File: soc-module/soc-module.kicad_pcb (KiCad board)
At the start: 2 copper layers, 56 x 31 mm, 17 parts, among them J1 Micro_SD_Card_Det_Hirose_DM3AT, J2 Conn_01x13, J3 Conn_01x14, SW1 Prog, SW2 Reset, U1 ATECC608A-SSHDA, U2 ESP32-WROVER-IE-16MB

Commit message: Ongoing
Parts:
- C1: renamed from C1^; value C -> 100nF
- C2, C3, C4: value C -> 100nF
- J1: value Micro_SD_Card_Det_Hirose_DM3AT -> Micro_SD
- J2: value Conn_01x13 -> East; footprint Connector_PinHeader_2.54mm:PinHeader_1x13_P2.54mm_Vertical -> Connector_PinHeader_2.54mm:PinHeader_1x14_P2.54mm_Vertical
- J3: value Conn_01x14 -> West
- R1, R2, R3, R4, R5, R6: value R -> 10k
- turned R1 to 180 degrees
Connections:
- J1 pad 3: SPI_0_MOSI -> IO23
- J1 pad 5: SPI_0_CLK -> IO18
- J1 pad 7: SPI_0_MISO -> IO19
- R1 pad 1: +3V3 -> IO0
- R1 pad 2: IO0 -> +3V3
- R3 pad 1: SPI_0_MISO -> IO19
- R4 pad 1: SPI_0_CLK -> IO18
- R5 pad 1: SPI_0_MOSI -> IO23
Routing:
- net IO23: track 15.3 -> 71.9 mm, vias 1 -> 3
- net IO19: track 19.1 -> 62.2 mm, vias 1 -> 3
- net IO18: track 20.0 -> 61.2 mm, vias 1 -> 3
- net SPI_0_MOSI: track 10.2 -> 0.00 mm, vias 1 -> 0
- net SPI_0_CLK: track 9.56 -> 0.00 mm, vias 1 -> 0
- net SPI_0_MISO: track 9.38 -> 0.00 mm, vias 1 -> 0
- net IO5: track 61.1 -> 60.1 mm
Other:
- board text added: "SPI PullUps"

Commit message: Ongoing Work. Still not ready for small and dedicated commits.
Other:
- board size 56 x 31 mm -> 56 x 30.4 mm
- board text added: "GC-SR-002"

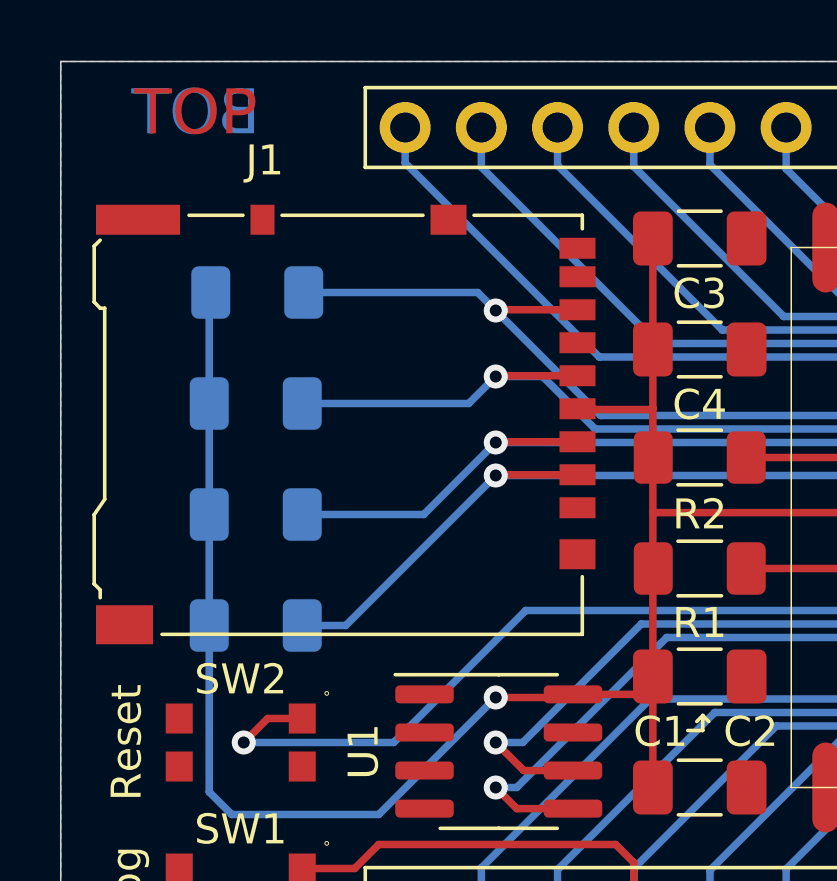
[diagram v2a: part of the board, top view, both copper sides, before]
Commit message: Use a cheaper SD card interface
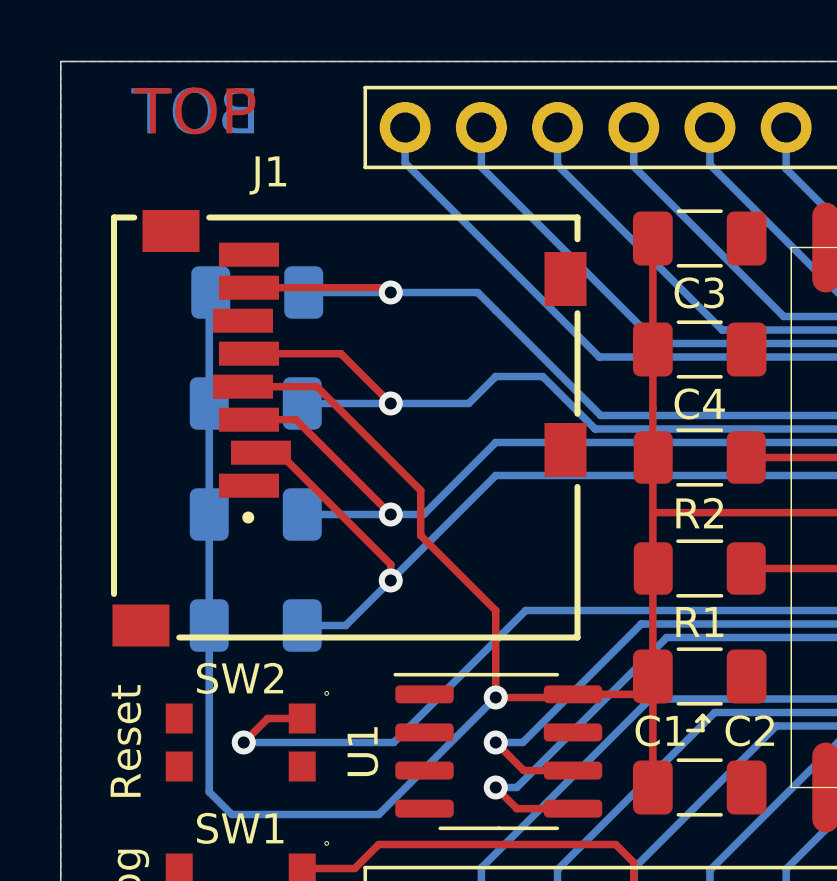
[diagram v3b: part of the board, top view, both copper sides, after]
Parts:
- J1: footprint Connector_Card:microSD_HC_Hirose_DM3AT-SF-PEJM5 -> footprints:GCT_MEM2061-01-188-00-A_REVA
- moved J1 0.10 mm to (129.5, 92.5)
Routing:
- net +3V3: track 97.3 -> 110.2 mm
- net IO5: track 60.1 -> 63.8 mm
- net IO23: track 71.9 -> 75.2 mm
- net IO18: track 61.2 -> 63.9 mm
- net IO19: track 62.2 -> 64.2 mm

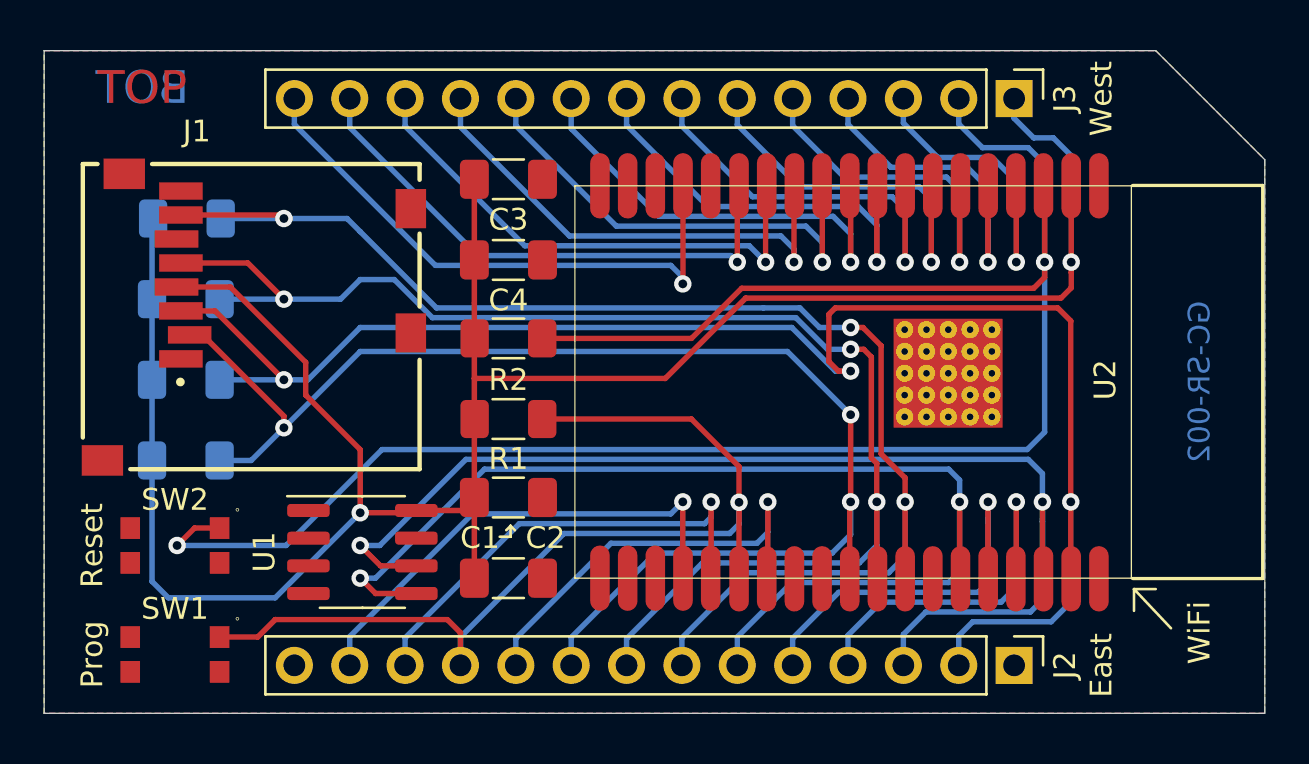
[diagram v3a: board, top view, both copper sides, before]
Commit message: Introduce new serial numbering scheme
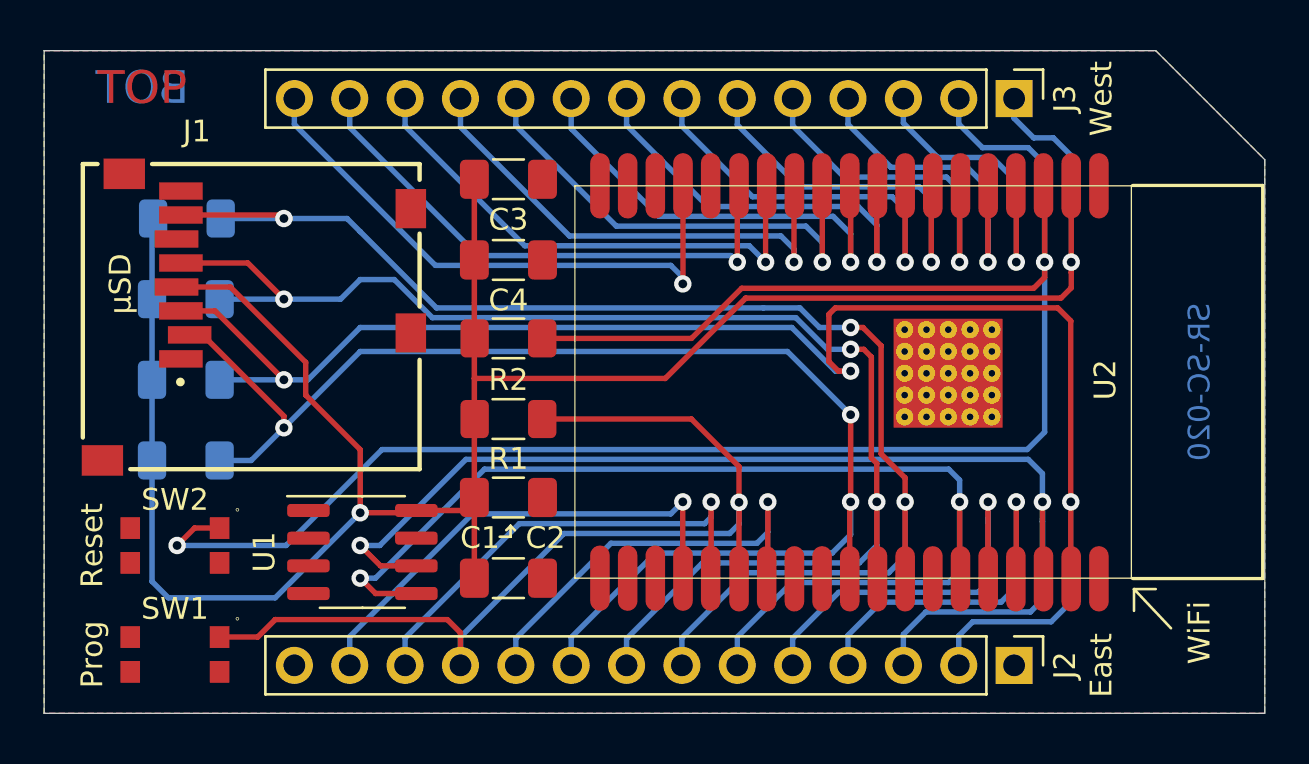
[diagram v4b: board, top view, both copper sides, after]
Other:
- board text added: "SR-SC-020"
- board text added: "Satellite SoC Module v2.0 GrayC GmbH https://docs.inoa.io"
- board text added: "µSD"
- board text removed: "GC-SR-002"
- board text removed: "Satellite SoC Module v2.0 GrayC GmbH"
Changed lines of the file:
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@@
   (general
     (thickness 1.6)
-    (drawings 18)
+    (drawings 19)
     (tracks 328)
     (zones 0)
@@
     )
   )
-  (gr_text GC-SR-002 (at 173 95.5 90) (layer B.Cu)
+  (gr_text µSD (at 123.5 91 90) (layer F.SilkS)
+    (effects (font (size 1 1) (thickness 0.15)))
+  )
+  (gr_text SR-SC-020 (at 173 95.5 90) (layer B.Cu)
     (effects (font (size 1 1) (thickness 0.15)) (justify mirror))
   )
@@
     (effects (font (size 1.5 1.5) (thickness 0.3)) (justify mirror))
   )
-  (gr_text "Satellite SoC Module v2.0\nGrayC GmbH" (at 147.5 95.2) (layer B.SilkS)
+  (gr_text "Satellite SoC Module v2.0\nGrayC GmbH\nhttps://docs.inoa.io" (at 146 95) (layer B.SilkS)
     (effects (font (size 1 1) (thickness 0.15)) (justify mirror))
   )

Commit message: Work on Ethernet module
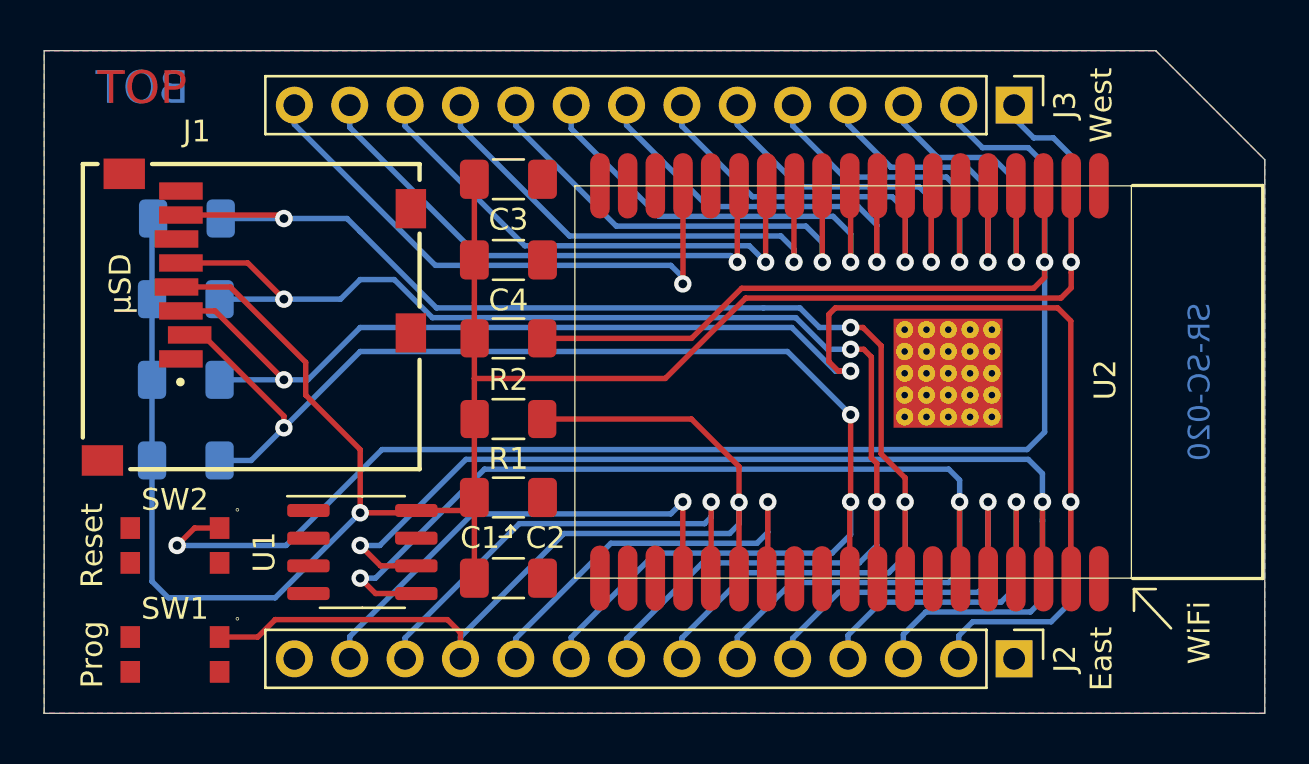
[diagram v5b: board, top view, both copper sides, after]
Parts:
- added G1: LOGO, images:grayc-logo-negative, B.Cu at (123.0, 107.3)
- moved J2 0.30 mm to (164.5, 108.2)
- moved J3 0.30 mm to (164.5, 82.8)

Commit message: Added OpenHardware Logo to PCBs
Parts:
- added G2: Logo_Open_Hardware_Small, Symbol:OSHW-Logo2_7.3x6mm_SilkScreen, B.Cu at (172.5, 106.0)

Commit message: Migrate Ethernet, SoC, Metering Modules to KiCad6
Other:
- net class Default removed

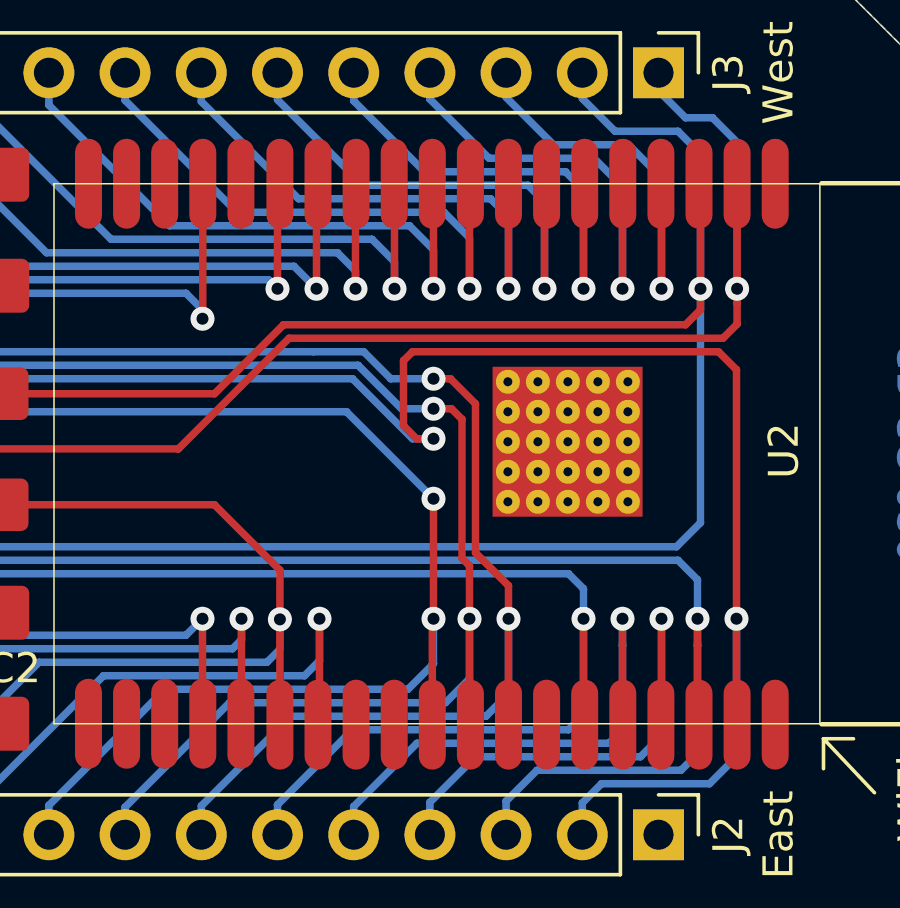
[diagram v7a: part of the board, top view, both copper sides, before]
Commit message: Trim further warnings and errors
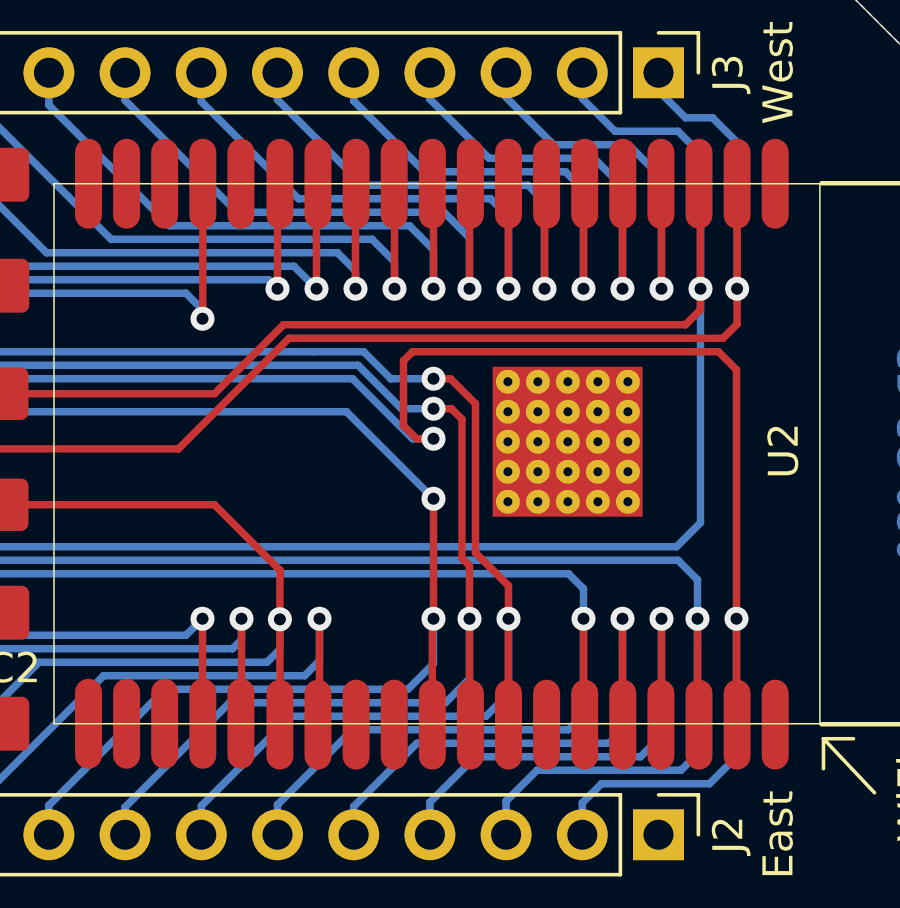
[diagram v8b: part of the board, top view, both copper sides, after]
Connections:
- net I2C_SCL renamed IO22
- net I2C_SDA renamed IO21
- J1 pad 1: Net-(J1-Pad1) -> unconnected-(J1-Pad1)
- J1 pad 10: Net-(J1-Pad10) -> unconnected-(J1-Pad10)
- J1 pad 8: Net-(J1-Pad8) -> unconnected-(J1-Pad8)
- J1 pad 9: Net-(J1-Pad9) -> unconnected-(J1-Pad9)
- J2 pad 14: Net-(J2-Pad14) -> unconnected-(J2-Pad14)
- U2 pad 17: Net-(U2-Pad17) -> unconnected-(U2-Pad17)
- U2 pad 18: Net-(U2-Pad18) -> unconnected-(U2-Pad18)
- U2 pad 19: Net-(U2-Pad19) -> unconnected-(U2-Pad19)
- U2 pad 20: Net-(U2-Pad20) -> unconnected-(U2-Pad20)
- U2 pad 21: Net-(U2-Pad21) -> unconnected-(U2-Pad21)
- U2 pad 22: Net-(U2-Pad22) -> unconnected-(U2-Pad22)
- U2 pad 27: Net-(U2-Pad27) -> unconnected-(U2-Pad27)
- U2 pad 28: Net-(U2-Pad28) -> unconnected-(U2-Pad28)
- U2 pad 32: Net-(U2-Pad32) -> unconnected-(U2-Pad32)
